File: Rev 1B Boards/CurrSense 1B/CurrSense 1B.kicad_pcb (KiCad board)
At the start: 4 copper layers, 135.8 x 56 mm, 48 parts, among them J1 Conn_01x01_Pin, J10 Conn_01x01_Pin, J13 Banana 2P, J14 Banana 2P, J15 Banana 2P, J2 Conn_01x01_Pin, J3 XT30_F, J4 Banana 2P, J5 Banana 2P, J6 XT30_F, J7 XT30_F, J8 Banana 2P, J9 XT30_F, Q1 BSC059N04LS6, Q2 BSC059N04LS6, U1 MAX4073T, U2 OPA551U, U3 TLV9301xDBV, U4 OPA551U, U5 TLV9301xDBV

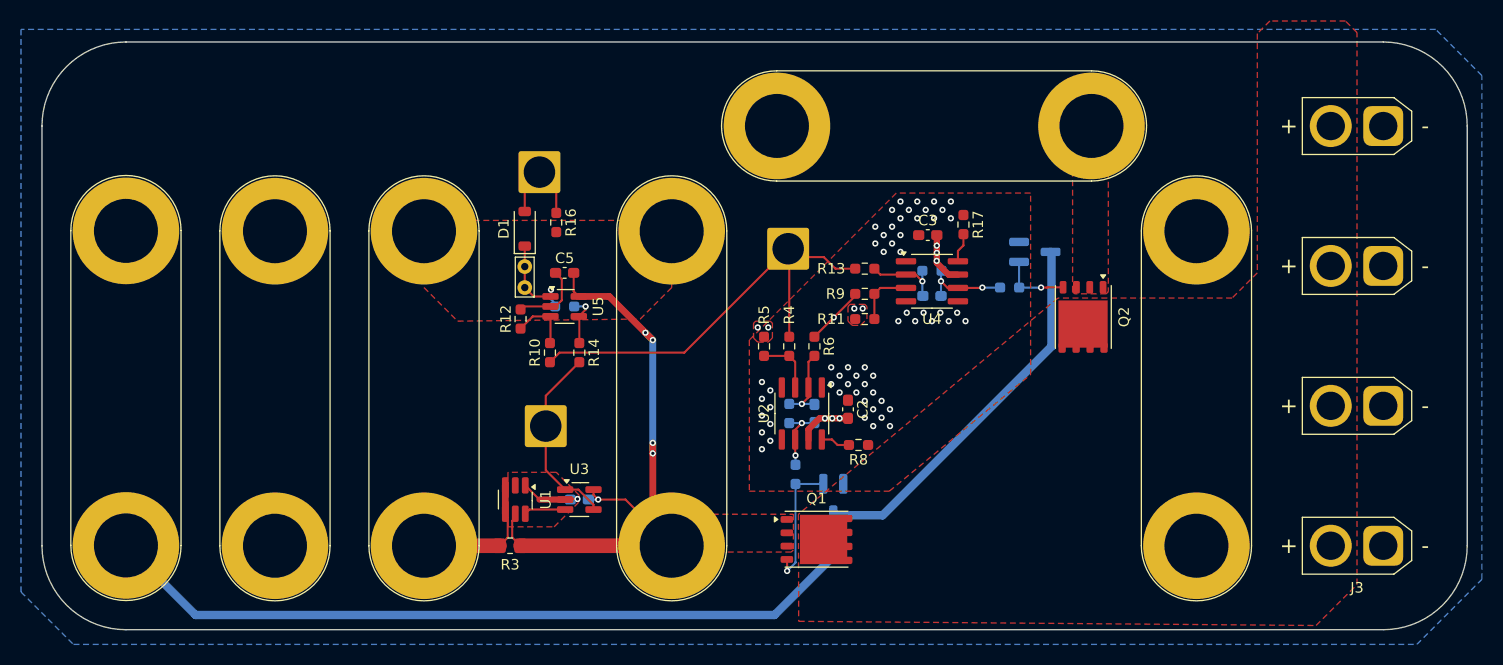
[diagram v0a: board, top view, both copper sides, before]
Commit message: Add labels + more test points
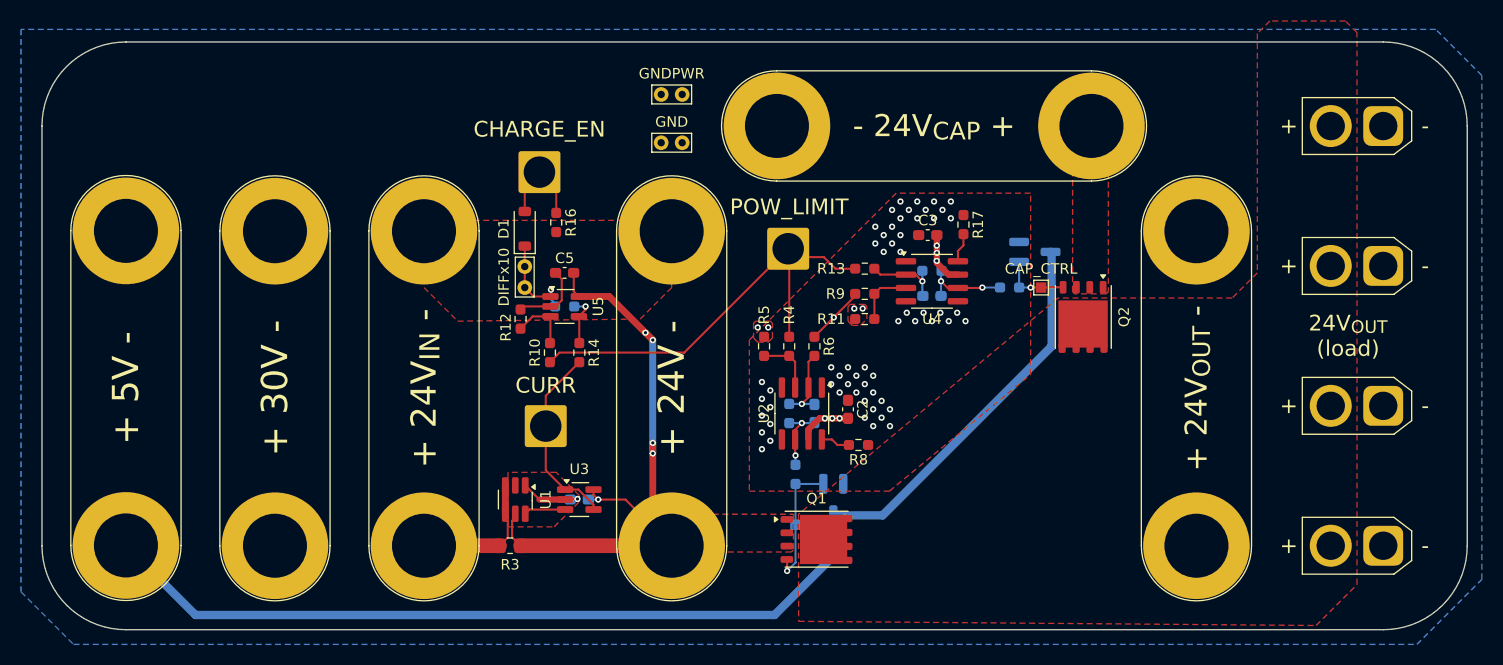
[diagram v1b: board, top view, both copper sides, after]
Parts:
- added TP2: V_{DIFF10}, TestPoint:TestPoint_Bridge_Pitch2.0mm_Drill0.7mm, F.Cu at (138.2, 76.8)
- added TP3: V_{DIFF10}, TestPoint:TestPoint_Bridge_Pitch2.0mm_Drill0.7mm, F.Cu at (138.2, 72.2)
- added TP4: V_{DIFF10}, TestPoint:TestPoint_Pad_1.0x1.0mm, F.Cu at (174.4, 90.6)
- added TP5: V_{DIFF10}, TestPoint:TestPoint_Pad_1.0x1.0mm, B.Cu at (151.0, 113.2)
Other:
- board text added: "+ 24V -"
- board text added: "+ 24V_{IN} -"
- board text added: "+ 24V_{OUT} -"
- board text added: "+ 30V -"
- board text added: "+ 5V -"
- board text added: "- 24V_{CAP} +"
- board text added: "24V_{OUT} (load)"
- board text added: "BAT_CTRL"
- board text added: "CAP_CTRL"
- board text added: "CHARGE_EN"
- board text added: "CURR"
- board text added: "DIFFx10"
- board text added: "GND"
- board text added: "GNDPWR"
- board text added: "POW_LIMIT"
